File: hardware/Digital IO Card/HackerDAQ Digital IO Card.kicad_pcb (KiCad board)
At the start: 2 copper layers, 90 x 90 mm, 8 parts, among them J1 MiniFit_Jr_5569_08A2, J2 MiniFit_Jr_5569_08A2, J3 MiniFit_Jr_5569_08A2, J9 LD15S33E4GX00LF, U4 M95320-RMN6

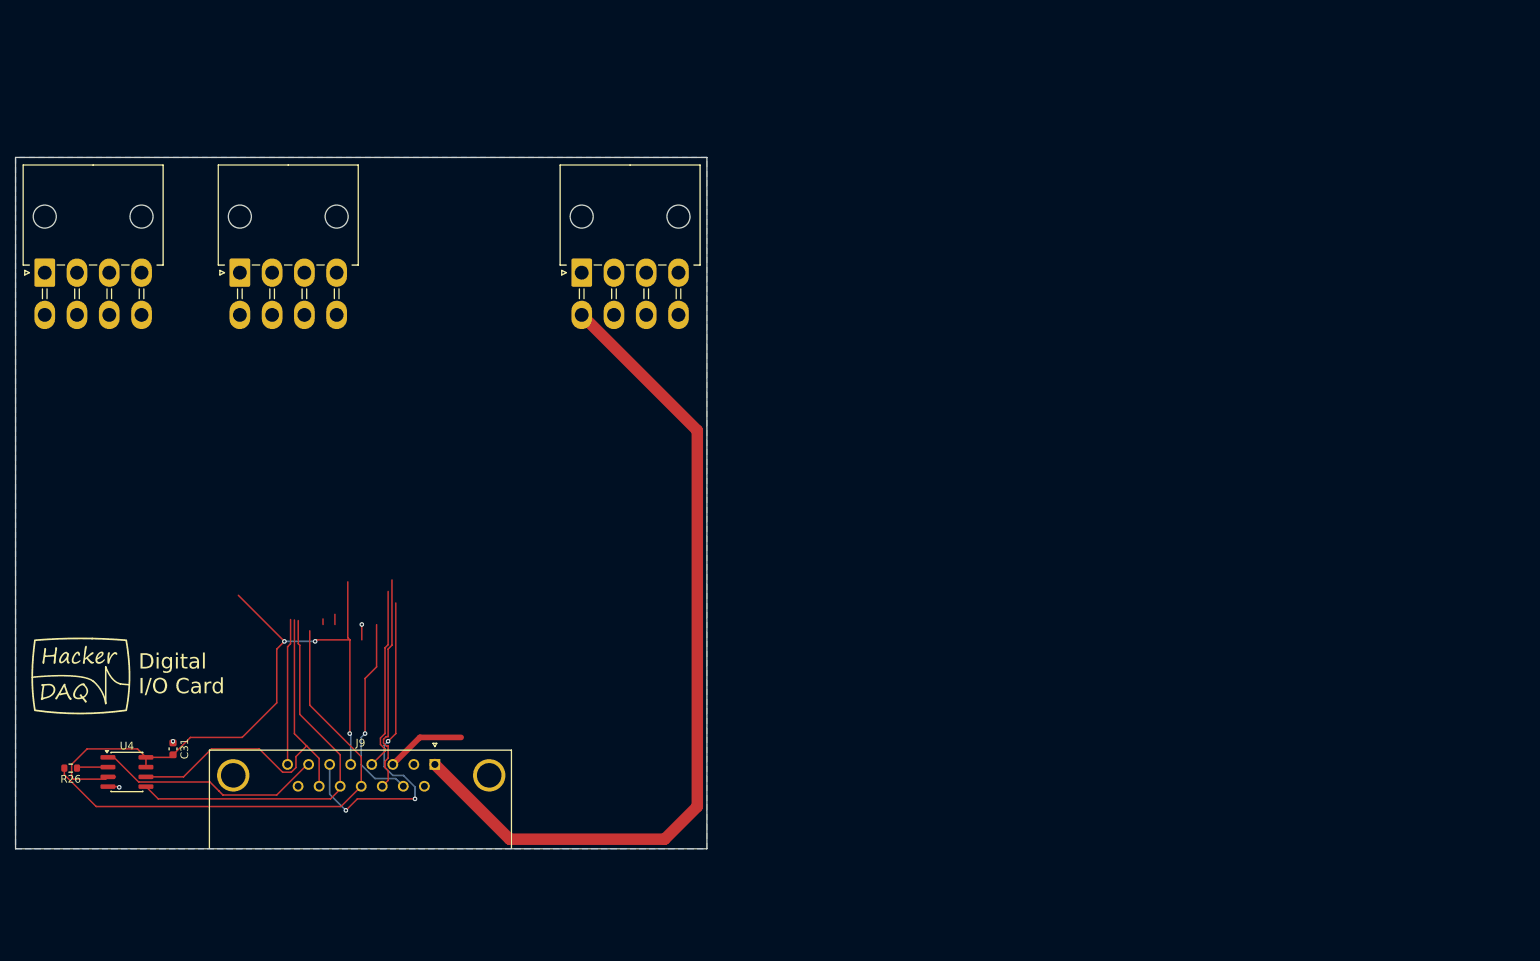
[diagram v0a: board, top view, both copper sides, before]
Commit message: DIO card initial schematic done
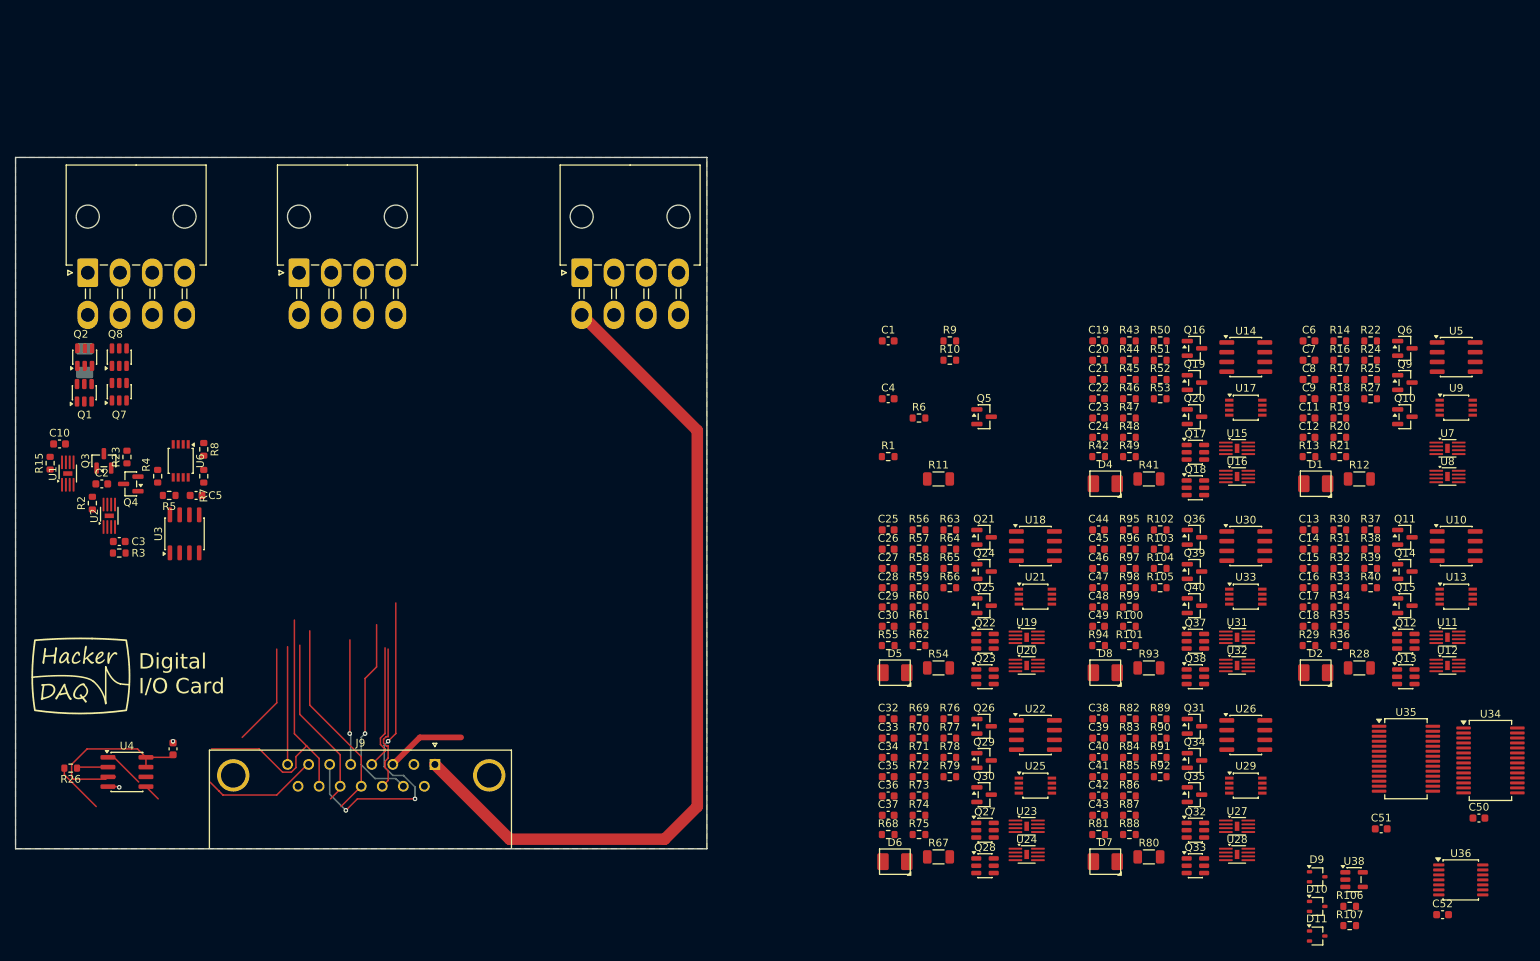
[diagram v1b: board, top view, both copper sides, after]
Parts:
- added C1: 1µF, Capacitor_SMD:C_0603_1608Metric, F.Cu at (163.6, 73.9)
- added C10: 1µF, Capacitor_SMD:C_0603_1608Metric, F.Cu at (55.7, 87.3)
- added C11: 1µF, Capacitor_SMD:C_0603_1608Metric, F.Cu at (218.4, 83.9)
- added C12: 100nF, Capacitor_SMD:C_0603_1608Metric, F.Cu at (218.4, 86.4)
- added C13: 100nF, Capacitor_SMD:C_0603_1608Metric, F.Cu at (218.4, 98.5)
- added C14: 1µF, Capacitor_SMD:C_0603_1608Metric, F.Cu at (218.4, 101.0)
- added C15: 1µF, Capacitor_SMD:C_0603_1608Metric, F.Cu at (218.4, 103.5)
- added C16: 1µF, Capacitor_SMD:C_0603_1608Metric, F.Cu at (218.4, 106.0)
- added C17: 1µF, Capacitor_SMD:C_0603_1608Metric, F.Cu at (218.4, 108.5)
- added C18: 100nF, Capacitor_SMD:C_0603_1608Metric, F.Cu at (218.4, 111.0)
- added C19: 100nF, Capacitor_SMD:C_0603_1608Metric, F.Cu at (191.0, 73.9)
- added C2: 1µF, Capacitor_SMD:C_0603_1608Metric, F.Cu at (61.2, 92.5)
- added C20: 1µF, Capacitor_SMD:C_0603_1608Metric, F.Cu at (191.0, 76.4)
- added C21: 1µF, Capacitor_SMD:C_0603_1608Metric, F.Cu at (191.0, 78.9)
- added C22: 1µF, Capacitor_SMD:C_0603_1608Metric, F.Cu at (191.0, 81.4)
- added C23: 1µF, Capacitor_SMD:C_0603_1608Metric, F.Cu at (191.0, 83.9)
- added C24: 100nF, Capacitor_SMD:C_0603_1608Metric, F.Cu at (191.0, 86.4)
- added C25: 100nF, Capacitor_SMD:C_0603_1608Metric, F.Cu at (163.6, 98.5)
- added C26: 1µF, Capacitor_SMD:C_0603_1608Metric, F.Cu at (163.6, 101.0)
- added C27: 1µF, Capacitor_SMD:C_0603_1608Metric, F.Cu at (163.6, 103.5)
- added C28: 1µF, Capacitor_SMD:C_0603_1608Metric, F.Cu at (163.6, 106.0)
- added C29: 1µF, Capacitor_SMD:C_0603_1608Metric, F.Cu at (163.6, 108.5)
- added C3: 1µF, Capacitor_SMD:C_0603_1608Metric, F.Cu at (63.5, 100.0)
- added C30: 100nF, Capacitor_SMD:C_0603_1608Metric, F.Cu at (163.6, 111.0)
- added C32: 100nF, Capacitor_SMD:C_0603_1608Metric, F.Cu at (163.6, 123.1)
- added C33: 1µF, Capacitor_SMD:C_0603_1608Metric, F.Cu at (163.6, 125.6)
- added C34: 1µF, Capacitor_SMD:C_0603_1608Metric, F.Cu at (163.6, 128.1)
- added C35: 1µF, Capacitor_SMD:C_0603_1608Metric, F.Cu at (163.6, 130.6)
- added C36: 1µF, Capacitor_SMD:C_0603_1608Metric, F.Cu at (163.6, 133.1)
- added C37: 100nF, Capacitor_SMD:C_0603_1608Metric, F.Cu at (163.6, 135.6)
- added C38: 100nF, Capacitor_SMD:C_0603_1608Metric, F.Cu at (191.0, 123.1)
- added C39: 1µF, Capacitor_SMD:C_0603_1608Metric, F.Cu at (191.0, 125.6)
- added C4: 100nF, Capacitor_SMD:C_0603_1608Metric, F.Cu at (163.6, 81.4)
- added C40: 1µF, Capacitor_SMD:C_0603_1608Metric, F.Cu at (191.0, 128.1)
- added C41: 1µF, Capacitor_SMD:C_0603_1608Metric, F.Cu at (191.0, 130.6)
- added C42: 1µF, Capacitor_SMD:C_0603_1608Metric, F.Cu at (191.0, 133.1)
- added C43: 100nF, Capacitor_SMD:C_0603_1608Metric, F.Cu at (191.0, 135.6)
- added C44: 100nF, Capacitor_SMD:C_0603_1608Metric, F.Cu at (191.0, 98.5)
- added C45: 1µF, Capacitor_SMD:C_0603_1608Metric, F.Cu at (191.0, 101.0)
- added C46: 1µF, Capacitor_SMD:C_0603_1608Metric, F.Cu at (191.0, 103.5)
- added C47: 1µF, Capacitor_SMD:C_0603_1608Metric, F.Cu at (191.0, 106.0)
- added C48: 1µF, Capacitor_SMD:C_0603_1608Metric, F.Cu at (191.0, 108.5)
- added C49: 100nF, Capacitor_SMD:C_0603_1608Metric, F.Cu at (191.0, 111.0)
- added C5: 100nF, Capacitor_SMD:C_0603_1608Metric, F.Cu at (73.5, 94.0)
- added C50: 100nF, Capacitor_SMD:C_0603_1608Metric, F.Cu at (240.5, 136.0)
- added C51: 100nF, Capacitor_SMD:C_0603_1608Metric, F.Cu at (227.8, 137.4)
- added C52: 100nF, Capacitor_SMD:C_0603_1608Metric, F.Cu at (235.8, 148.6)
- added C6: 100nF, Capacitor_SMD:C_0603_1608Metric, F.Cu at (218.4, 73.9)
- added C7: 1µF, Capacitor_SMD:C_0603_1608Metric, F.Cu at (218.4, 76.4)
- added C8: 1µF, Capacitor_SMD:C_0603_1608Metric, F.Cu at (218.4, 78.9)
- added C9: 1µF, Capacitor_SMD:C_0603_1608Metric, F.Cu at (218.4, 81.4)
- added D1: AA3528SURSK, ColorLEDs:AA3528, F.Cu at (219.2, 92.5)
- added D10: BAT54W, Package_TO_SOT_SMD:SOT-323_SC-70, F.Cu at (219.4, 147.5)
- added D11: BAT54W, Package_TO_SOT_SMD:SOT-323_SC-70, F.Cu at (219.4, 151.4)
- added D2: AA3528SURSK, ColorLEDs:AA3528, F.Cu at (219.2, 117.1)
- added D3: AA3528SURSK, ColorLEDs:AA3528, B.Cu at (59.0, 76.5)
- added D4: AA3528SURSK, ColorLEDs:AA3528, F.Cu at (191.9, 92.5)
- added D5: AA3528SURSK, ColorLEDs:AA3528, F.Cu at (164.5, 117.1)
- added D6: AA3528SURSK, ColorLEDs:AA3528, F.Cu at (164.5, 141.7)
- added D7: AA3528SURSK, ColorLEDs:AA3528, F.Cu at (191.9, 141.7)
- added D8: AA3528SURSK, ColorLEDs:AA3528, F.Cu at (191.9, 117.1)
- added D9: BAT54W, Package_TO_SOT_SMD:SOT-323_SC-70, F.Cu at (219.4, 143.6)
- added Q1: RVQ040N05, Package_TO_SOT_SMD:SOT-23-6, F.Cu at (59.0, 80.6)
- added Q10: 2N7002, Package_TO_SOT_SMD:SOT-23, F.Cu at (230.9, 83.8)
- added Q11: 2N7002, Package_TO_SOT_SMD:SOT-23, F.Cu at (230.9, 99.5)
- added Q12: RVQ040N05, Package_TO_SOT_SMD:SOT-23-6, F.Cu at (231.0, 113.0)
- added Q13: RVQ040N05, Package_TO_SOT_SMD:SOT-23-6, F.Cu at (231.0, 117.6)
- added Q14: 2N7002, Package_TO_SOT_SMD:SOT-23, F.Cu at (230.9, 103.9)
- added Q15: 2N7002, Package_TO_SOT_SMD:SOT-23, F.Cu at (230.9, 108.4)
- added Q16: 2N7002, Package_TO_SOT_SMD:SOT-23, F.Cu at (203.5, 74.9)
- added Q17: RVQ040N05, Package_TO_SOT_SMD:SOT-23-6, F.Cu at (203.6, 88.4)
- added Q18: RVQ040N05, Package_TO_SOT_SMD:SOT-23-6, F.Cu at (203.6, 93.0)
- added Q19: 2N7002, Package_TO_SOT_SMD:SOT-23, F.Cu at (203.5, 79.3)
- added Q2: RVQ040N05, Package_TO_SOT_SMD:SOT-23-6, F.Cu at (59.0, 76.0)
- added Q20: 2N7002, Package_TO_SOT_SMD:SOT-23, F.Cu at (203.5, 83.8)
- added Q21: 2N7002, Package_TO_SOT_SMD:SOT-23, F.Cu at (176.1, 99.5)
- added Q22: RVQ040N05, Package_TO_SOT_SMD:SOT-23-6, F.Cu at (176.2, 113.0)
- added Q23: RVQ040N05, Package_TO_SOT_SMD:SOT-23-6, F.Cu at (176.2, 117.6)
- added Q24: 2N7002, Package_TO_SOT_SMD:SOT-23, F.Cu at (176.1, 103.9)
- added Q25: 2N7002, Package_TO_SOT_SMD:SOT-23, F.Cu at (176.1, 108.4)
- added Q26: 2N7002, Package_TO_SOT_SMD:SOT-23, F.Cu at (176.1, 124.1)
- added Q27: RVQ040N05, Package_TO_SOT_SMD:SOT-23-6, F.Cu at (176.2, 137.6)
- added Q28: RVQ040N05, Package_TO_SOT_SMD:SOT-23-6, F.Cu at (176.2, 142.2)
- added Q29: 2N7002, Package_TO_SOT_SMD:SOT-23, F.Cu at (176.1, 128.5)
- added Q3: 2N7002, Package_TO_SOT_SMD:SOT-23, F.Cu at (61.5, 89.5)
- added Q30: 2N7002, Package_TO_SOT_SMD:SOT-23, F.Cu at (176.1, 133.0)
- added Q31: 2N7002, Package_TO_SOT_SMD:SOT-23, F.Cu at (203.5, 124.1)
- added Q32: RVQ040N05, Package_TO_SOT_SMD:SOT-23-6, F.Cu at (203.6, 137.6)
- added Q33: RVQ040N05, Package_TO_SOT_SMD:SOT-23-6, F.Cu at (203.6, 142.2)
- added Q34: 2N7002, Package_TO_SOT_SMD:SOT-23, F.Cu at (203.5, 128.5)
- added Q35: 2N7002, Package_TO_SOT_SMD:SOT-23, F.Cu at (203.5, 133.0)
- added Q36: 2N7002, Package_TO_SOT_SMD:SOT-23, F.Cu at (203.5, 99.5)
- added Q37: RVQ040N05, Package_TO_SOT_SMD:SOT-23-6, F.Cu at (203.6, 113.0)
- added Q38: RVQ040N05, Package_TO_SOT_SMD:SOT-23-6, F.Cu at (203.6, 117.6)
- added Q39: 2N7002, Package_TO_SOT_SMD:SOT-23, F.Cu at (203.5, 103.9)
- added Q4: 2N7002, Package_TO_SOT_SMD:SOT-23, F.Cu at (65.0, 92.5)
- added Q40: 2N7002, Package_TO_SOT_SMD:SOT-23, F.Cu at (203.5, 108.4)
- added Q5: 2N7002, Package_TO_SOT_SMD:SOT-23, F.Cu at (176.1, 83.8)
- added Q6: 2N7002, Package_TO_SOT_SMD:SOT-23, F.Cu at (230.9, 74.9)
- added Q7: RVQ040N05, Package_TO_SOT_SMD:SOT-23-6, F.Cu at (63.5, 80.5)
- added Q8: RVQ040N05, Package_TO_SOT_SMD:SOT-23-6, F.Cu at (63.5, 76.0)
- added Q9: 2N7002, Package_TO_SOT_SMD:SOT-23, F.Cu at (230.9, 79.3)
- added R1: 2.2, Resistor_SMD:R_0603_1608Metric, F.Cu at (163.6, 88.9)
- added R10: 14.7k, Resistor_SMD:R_0603_1608Metric, F.Cu at (171.6, 76.4)
- added R100: 14.7k, Resistor_SMD:R_0603_1608Metric, F.Cu at (195.0, 111.0)
- added R101: 1, Resistor_SMD:R_0603_1608Metric, F.Cu at (195.0, 113.5)
- added R102: 1, Resistor_SMD:R_0603_1608Metric, F.Cu at (199.0, 98.5)
- added R103: 133k, Resistor_SMD:R_0603_1608Metric, F.Cu at (199.0, 101.0)
- added R104: 33.2k, Resistor_SMD:R_0603_1608Metric, F.Cu at (199.0, 103.5)
- added R105: 10k, Resistor_SMD:R_0603_1608Metric, F.Cu at (199.0, 106.0)
- added R106: 10k, Resistor_SMD:R_0603_1608Metric, F.Cu at (223.7, 147.5)
- added R107: 33, Resistor_SMD:R_0603_1608Metric, F.Cu at (223.7, 150.0)
- added R11: 150, Resistor_SMD:R_1206_3216Metric, F.Cu at (170.2, 91.9)
- added R12: 150, Resistor_SMD:R_1206_3216Metric, F.Cu at (224.9, 91.9)
- added R13: 10k, Resistor_SMD:R_0603_1608Metric, F.Cu at (218.4, 88.9)
- added R14: 75k, Resistor_SMD:R_0603_1608Metric, F.Cu at (222.4, 73.9)
- added R15: 1, Resistor_SMD:R_0603_1608Metric, F.Cu at (54.5, 89.8)
- added R16: 2.2, Resistor_SMD:R_0603_1608Metric, F.Cu at (222.4, 76.4)
- added R17: 2.2, Resistor_SMD:R_0603_1608Metric, F.Cu at (222.4, 78.9)
- added R18: 30k, Resistor_SMD:R_0603_1608Metric, F.Cu at (222.4, 81.4)
- added R19: 133k, Resistor_SMD:R_0603_1608Metric, F.Cu at (222.4, 83.9)
- added R2: 1, Resistor_SMD:R_0603_1608Metric, F.Cu at (60.0, 95.0)
- added R20: 14.7k, Resistor_SMD:R_0603_1608Metric, F.Cu at (222.4, 86.4)
- added R21: 1, Resistor_SMD:R_0603_1608Metric, F.Cu at (222.4, 88.9)
- added R22: 1, Resistor_SMD:R_0603_1608Metric, F.Cu at (226.4, 73.9)
- added R23: 10k, Resistor_SMD:R_0603_1608Metric, F.Cu at (64.5, 89.0)
- added R24: 133k, Resistor_SMD:R_0603_1608Metric, F.Cu at (226.4, 76.4)
- added R25: 33.2k, Resistor_SMD:R_0603_1608Metric, F.Cu at (226.4, 78.9)
- added R27: 10k, Resistor_SMD:R_0603_1608Metric, F.Cu at (226.4, 81.4)
- added R28: 150, Resistor_SMD:R_1206_3216Metric, F.Cu at (224.9, 116.5)
- added R29: 10k, Resistor_SMD:R_0603_1608Metric, F.Cu at (218.4, 113.5)
- added R3: 2.2, Resistor_SMD:R_0603_1608Metric, F.Cu at (63.5, 101.5)
- added R30: 75k, Resistor_SMD:R_0603_1608Metric, F.Cu at (222.4, 98.5)
- added R31: 2.2, Resistor_SMD:R_0603_1608Metric, F.Cu at (222.4, 101.0)
- added R32: 2.2, Resistor_SMD:R_0603_1608Metric, F.Cu at (222.4, 103.5)
- added R33: 30k, Resistor_SMD:R_0603_1608Metric, F.Cu at (222.4, 106.0)
- added R34: 133k, Resistor_SMD:R_0603_1608Metric, F.Cu at (222.4, 108.5)
- added R35: 14.7k, Resistor_SMD:R_0603_1608Metric, F.Cu at (222.4, 111.0)
- added R36: 1, Resistor_SMD:R_0603_1608Metric, F.Cu at (222.4, 113.5)
- added R37: 1, Resistor_SMD:R_0603_1608Metric, F.Cu at (226.4, 98.5)
- added R38: 133k, Resistor_SMD:R_0603_1608Metric, F.Cu at (226.4, 101.0)
- added R39: 33.2k, Resistor_SMD:R_0603_1608Metric, F.Cu at (226.4, 103.5)
- added R4: 75k, Resistor_SMD:R_0603_1608Metric, F.Cu at (68.5, 91.5)
- added R40: 10k, Resistor_SMD:R_0603_1608Metric, F.Cu at (226.4, 106.0)
- added R41: 150, Resistor_SMD:R_1206_3216Metric, F.Cu at (197.5, 91.9)
- added R42: 10k, Resistor_SMD:R_0603_1608Metric, F.Cu at (191.0, 88.9)
- added R43: 75k, Resistor_SMD:R_0603_1608Metric, F.Cu at (195.0, 73.9)
- added R44: 2.2, Resistor_SMD:R_0603_1608Metric, F.Cu at (195.0, 76.4)
- added R45: 2.2, Resistor_SMD:R_0603_1608Metric, F.Cu at (195.0, 78.9)
- added R46: 30k, Resistor_SMD:R_0603_1608Metric, F.Cu at (195.0, 81.4)
- added R47: 133k, Resistor_SMD:R_0603_1608Metric, F.Cu at (195.0, 83.9)
- added R48: 14.7k, Resistor_SMD:R_0603_1608Metric, F.Cu at (195.0, 86.4)
- added R49: 1, Resistor_SMD:R_0603_1608Metric, F.Cu at (195.0, 88.9)
- added R5: 30k, Resistor_SMD:R_0603_1608Metric, F.Cu at (70.0, 94.0)
- added R50: 1, Resistor_SMD:R_0603_1608Metric, F.Cu at (199.0, 73.9)
- added R51: 133k, Resistor_SMD:R_0603_1608Metric, F.Cu at (199.0, 76.4)
- added R52: 33.2k, Resistor_SMD:R_0603_1608Metric, F.Cu at (199.0, 78.9)
- added R53: 10k, Resistor_SMD:R_0603_1608Metric, F.Cu at (199.0, 81.4)
- added R54: 150, Resistor_SMD:R_1206_3216Metric, F.Cu at (170.2, 116.5)
- added R55: 10k, Resistor_SMD:R_0603_1608Metric, F.Cu at (163.6, 113.5)
- added R56: 75k, Resistor_SMD:R_0603_1608Metric, F.Cu at (167.6, 98.5)
- added R57: 2.2, Resistor_SMD:R_0603_1608Metric, F.Cu at (167.6, 101.0)
- added R58: 2.2, Resistor_SMD:R_0603_1608Metric, F.Cu at (167.6, 103.5)
- added R59: 30k, Resistor_SMD:R_0603_1608Metric, F.Cu at (167.6, 106.0)
- added R6: 10k, Resistor_SMD:R_0603_1608Metric, F.Cu at (167.6, 83.9)
- added R60: 133k, Resistor_SMD:R_0603_1608Metric, F.Cu at (167.6, 108.5)
- added R61: 14.7k, Resistor_SMD:R_0603_1608Metric, F.Cu at (167.6, 111.0)
- added R62: 1, Resistor_SMD:R_0603_1608Metric, F.Cu at (167.6, 113.5)
- added R63: 1, Resistor_SMD:R_0603_1608Metric, F.Cu at (171.6, 98.5)
- added R64: 133k, Resistor_SMD:R_0603_1608Metric, F.Cu at (171.6, 101.0)
- added R65: 33.2k, Resistor_SMD:R_0603_1608Metric, F.Cu at (171.6, 103.5)
- added R66: 10k, Resistor_SMD:R_0603_1608Metric, F.Cu at (171.6, 106.0)
- added R67: 150, Resistor_SMD:R_1206_3216Metric, F.Cu at (170.2, 141.1)
- added R68: 10k, Resistor_SMD:R_0603_1608Metric, F.Cu at (163.6, 138.1)
- added R69: 75k, Resistor_SMD:R_0603_1608Metric, F.Cu at (167.6, 123.1)
- added R7: 33.2k, Resistor_SMD:R_0603_1608Metric, F.Cu at (74.5, 91.5)
- added R70: 2.2, Resistor_SMD:R_0603_1608Metric, F.Cu at (167.6, 125.6)
- added R71: 2.2, Resistor_SMD:R_0603_1608Metric, F.Cu at (167.6, 128.1)
- added R72: 30k, Resistor_SMD:R_0603_1608Metric, F.Cu at (167.6, 130.6)
- added R73: 133k, Resistor_SMD:R_0603_1608Metric, F.Cu at (167.6, 133.1)
- added R74: 14.7k, Resistor_SMD:R_0603_1608Metric, F.Cu at (167.6, 135.6)
- added R75: 1, Resistor_SMD:R_0603_1608Metric, F.Cu at (167.6, 138.1)
- added R76: 1, Resistor_SMD:R_0603_1608Metric, F.Cu at (171.6, 123.1)
- added R77: 133k, Resistor_SMD:R_0603_1608Metric, F.Cu at (171.6, 125.6)
- added R78: 33.2k, Resistor_SMD:R_0603_1608Metric, F.Cu at (171.6, 128.1)
- added R79: 10k, Resistor_SMD:R_0603_1608Metric, F.Cu at (171.6, 130.6)
- added R8: 133k, Resistor_SMD:R_0603_1608Metric, F.Cu at (74.5, 88.0)
- added R80: 150, Resistor_SMD:R_1206_3216Metric, F.Cu at (197.5, 141.1)
- added R81: 10k, Resistor_SMD:R_0603_1608Metric, F.Cu at (191.0, 138.1)
- added R82: 75k, Resistor_SMD:R_0603_1608Metric, F.Cu at (195.0, 123.1)
- added R83: 2.2, Resistor_SMD:R_0603_1608Metric, F.Cu at (195.0, 125.6)
- added R84: 2.2, Resistor_SMD:R_0603_1608Metric, F.Cu at (195.0, 128.1)
- added R85: 30k, Resistor_SMD:R_0603_1608Metric, F.Cu at (195.0, 130.6)
- added R86: 133k, Resistor_SMD:R_0603_1608Metric, F.Cu at (195.0, 133.1)
- added R87: 14.7k, Resistor_SMD:R_0603_1608Metric, F.Cu at (195.0, 135.6)
- added R88: 1, Resistor_SMD:R_0603_1608Metric, F.Cu at (195.0, 138.1)
- added R89: 1, Resistor_SMD:R_0603_1608Metric, F.Cu at (199.0, 123.1)
- added R9: 133k, Resistor_SMD:R_0603_1608Metric, F.Cu at (171.6, 73.9)
- added R90: 133k, Resistor_SMD:R_0603_1608Metric, F.Cu at (199.0, 125.6)
- added R91: 33.2k, Resistor_SMD:R_0603_1608Metric, F.Cu at (199.0, 128.1)
- added R92: 10k, Resistor_SMD:R_0603_1608Metric, F.Cu at (199.0, 130.6)
- added R93: 150, Resistor_SMD:R_1206_3216Metric, F.Cu at (197.5, 116.5)
- added R94: 10k, Resistor_SMD:R_0603_1608Metric, F.Cu at (191.0, 113.5)
- added R95: 75k, Resistor_SMD:R_0603_1608Metric, F.Cu at (195.0, 98.5)
- added R96: 2.2, Resistor_SMD:R_0603_1608Metric, F.Cu at (195.0, 101.0)
- added R97: 2.2, Resistor_SMD:R_0603_1608Metric, F.Cu at (195.0, 103.5)
- added R98: 30k, Resistor_SMD:R_0603_1608Metric, F.Cu at (195.0, 106.0)
- added R99: 133k, Resistor_SMD:R_0603_1608Metric, F.Cu at (195.0, 108.5)
- added U1: RT9624CGQWA, Project Library:DFN-8-1EP_2x2mm_P0.5mm_EP0.6x1.2mm_LeadsExtended, F.Cu at (56.8, 91.2)
- added U10: LM311DR, Package_SO:SOIC-8_3.9x4.9mm_P1.27mm, F.Cu at (237.5, 100.6)
- added U11: RT9624CGQWA, Project Library:DFN-8-1EP_2x2mm_P0.5mm_EP0.6x1.2mm_LeadsExtended, F.Cu at (236.4, 112.5)
- added U12: RT9624CGQWA, Project Library:DFN-8-1EP_2x2mm_P0.5mm_EP0.6x1.2mm_LeadsExtended, F.Cu at (236.4, 116.1)
- added U13: LM358, Package_SO:TSSOP-8_3x3mm_P0.65mm, F.Cu at (237.5, 107.2)
- added U14: LM311DR, Package_SO:SOIC-8_3.9x4.9mm_P1.27mm, F.Cu at (210.2, 76.0)
- added U15: RT9624CGQWA, Project Library:DFN-8-1EP_2x2mm_P0.5mm_EP0.6x1.2mm_LeadsExtended, F.Cu at (209.0, 87.9)
- added U16: RT9624CGQWA, Project Library:DFN-8-1EP_2x2mm_P0.5mm_EP0.6x1.2mm_LeadsExtended, F.Cu at (209.0, 91.5)
- added U17: LM358, Package_SO:TSSOP-8_3x3mm_P0.65mm, F.Cu at (210.2, 82.6)
- added U18: LM311DR, Package_SO:SOIC-8_3.9x4.9mm_P1.27mm, F.Cu at (182.8, 100.6)
- added U19: RT9624CGQWA, Project Library:DFN-8-1EP_2x2mm_P0.5mm_EP0.6x1.2mm_LeadsExtended, F.Cu at (181.6, 112.5)
- added U2: RT9624CGQWA, Project Library:DFN-8-1EP_2x2mm_P0.5mm_EP0.6x1.2mm_LeadsExtended, F.Cu at (62.2, 96.7)
- added U20: RT9624CGQWA, Project Library:DFN-8-1EP_2x2mm_P0.5mm_EP0.6x1.2mm_LeadsExtended, F.Cu at (181.6, 116.1)
- added U21: LM358, Package_SO:TSSOP-8_3x3mm_P0.65mm, F.Cu at (182.8, 107.2)
- added U22: LM311DR, Package_SO:SOIC-8_3.9x4.9mm_P1.27mm, F.Cu at (182.8, 125.2)
- added U23: RT9624CGQWA, Project Library:DFN-8-1EP_2x2mm_P0.5mm_EP0.6x1.2mm_LeadsExtended, F.Cu at (181.6, 137.1)
- added U24: RT9624CGQWA, Project Library:DFN-8-1EP_2x2mm_P0.5mm_EP0.6x1.2mm_LeadsExtended, F.Cu at (181.6, 140.7)
- added U25: LM358, Package_SO:TSSOP-8_3x3mm_P0.65mm, F.Cu at (182.8, 131.8)
- added U26: LM311DR, Package_SO:SOIC-8_3.9x4.9mm_P1.27mm, F.Cu at (210.2, 125.2)
- added U27: RT9624CGQWA, Project Library:DFN-8-1EP_2x2mm_P0.5mm_EP0.6x1.2mm_LeadsExtended, F.Cu at (209.0, 137.1)
- added U28: RT9624CGQWA, Project Library:DFN-8-1EP_2x2mm_P0.5mm_EP0.6x1.2mm_LeadsExtended, F.Cu at (209.0, 140.7)
- added U29: LM358, Package_SO:TSSOP-8_3x3mm_P0.65mm, F.Cu at (210.2, 131.8)
- added U3: LM311DR, Package_SO:SOIC-8_3.9x4.9mm_P1.27mm, F.Cu at (72.0, 99.0)
- added U30: LM311DR, Package_SO:SOIC-8_3.9x4.9mm_P1.27mm, F.Cu at (210.2, 100.6)
- added U31: RT9624CGQWA, Project Library:DFN-8-1EP_2x2mm_P0.5mm_EP0.6x1.2mm_LeadsExtended, F.Cu at (209.0, 112.5)
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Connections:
- C31 pad 1: +3.3V -> +5V
- J1 pad 1: V_LOGIC -> /V_{LOGIC}_PORTA
- J1 pad 2: V_LOGIC -> /V_{LOGIC}_PORTB
- J2 pad 1: unconnected-(J2-Pin_1-Pad1) -> GND
- J2 pad 2: unconnected-(J2-Pin_2-Pad2) -> GND
- J2 pad 3: unconnected-(J2-Pin_3-Pad3) -> GND
- J2 pad 4: unconnected-(J2-Pin_4-Pad4) -> GND
- J2 pad 5: unconnected-(J2-Pin_5-Pad5) -> /DIOA0
- J2 pad 6: unconnected-(J2-Pin_6-Pad6) -> /DIOA1
- J2 pad 7: unconnected-(J2-Pin_7-Pad7) -> /DIOA2
- J2 pad 8: unconnected-(J2-Pin_8-Pad8) -> /DIOA3
- J3 pad 1: unconnected-(J3-Pin_1-Pad1) -> GND
- J3 pad 2: unconnected-(J3-Pin_2-Pad2) -> GND
- J3 pad 3: unconnected-(J3-Pin_3-Pad3) -> GND
- J3 pad 4: unconnected-(J3-Pin_4-Pad4) -> GND
- J3 pad 5: unconnected-(J3-Pin_5-Pad5) -> /DIOB0
- J3 pad 6: unconnected-(J3-Pin_6-Pad6) -> /DIOB1
- J3 pad 7: unconnected-(J3-Pin_7-Pad7) -> /DIOB2
- J3 pad 8: unconnected-(J3-Pin_8-Pad8) -> /DIOB3
- J9 pad 12: /B2B Connector Card Side/SPI.MISO -> /SPI.MISO
- J9 pad 13: /B2B Connector Card Side/SPI.MOSI -> /SPI.MOSI
- J9 pad 14: /B2B Connector Card Side/SPI.SCLK -> /SPI.SCLK
- J9 pad 15: /B2B Connector Card Side/CS1 -> /~{CS}1
- J9 pad 6: /B2B Connector Card Side/~{RESET} -> /~{RESET}
- J9 pad 7: /B2B Connector Card Side/CS2 -> /~{CS}2
- J9 pad 8: /B2B Connector Card Side/CS0 -> /~{CS}0
- R26 pad 2: /B2B Connector Card Side/SPI.MISO -> /IOExpanderA/SPI_5V.MISO
- U4 pad 1: /B2B Connector Card Side/CS2 -> /LevelShifter/~{CS_5V}2
- U4 pad 3: +3.3V -> +5V
- U4 pad 5: /B2B Connector Card Side/SPI.MOSI -> /IOExpanderA/SPI_5V.MOSI
- U4 pad 6: /B2B Connector Card Side/SPI.SCLK -> /IOExpanderA/SPI_5V.SCLK
- U4 pad 7: +3.3V -> +5V
- U4 pad 8: +3.3V -> +5V
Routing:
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
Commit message: Start redoing DIO card
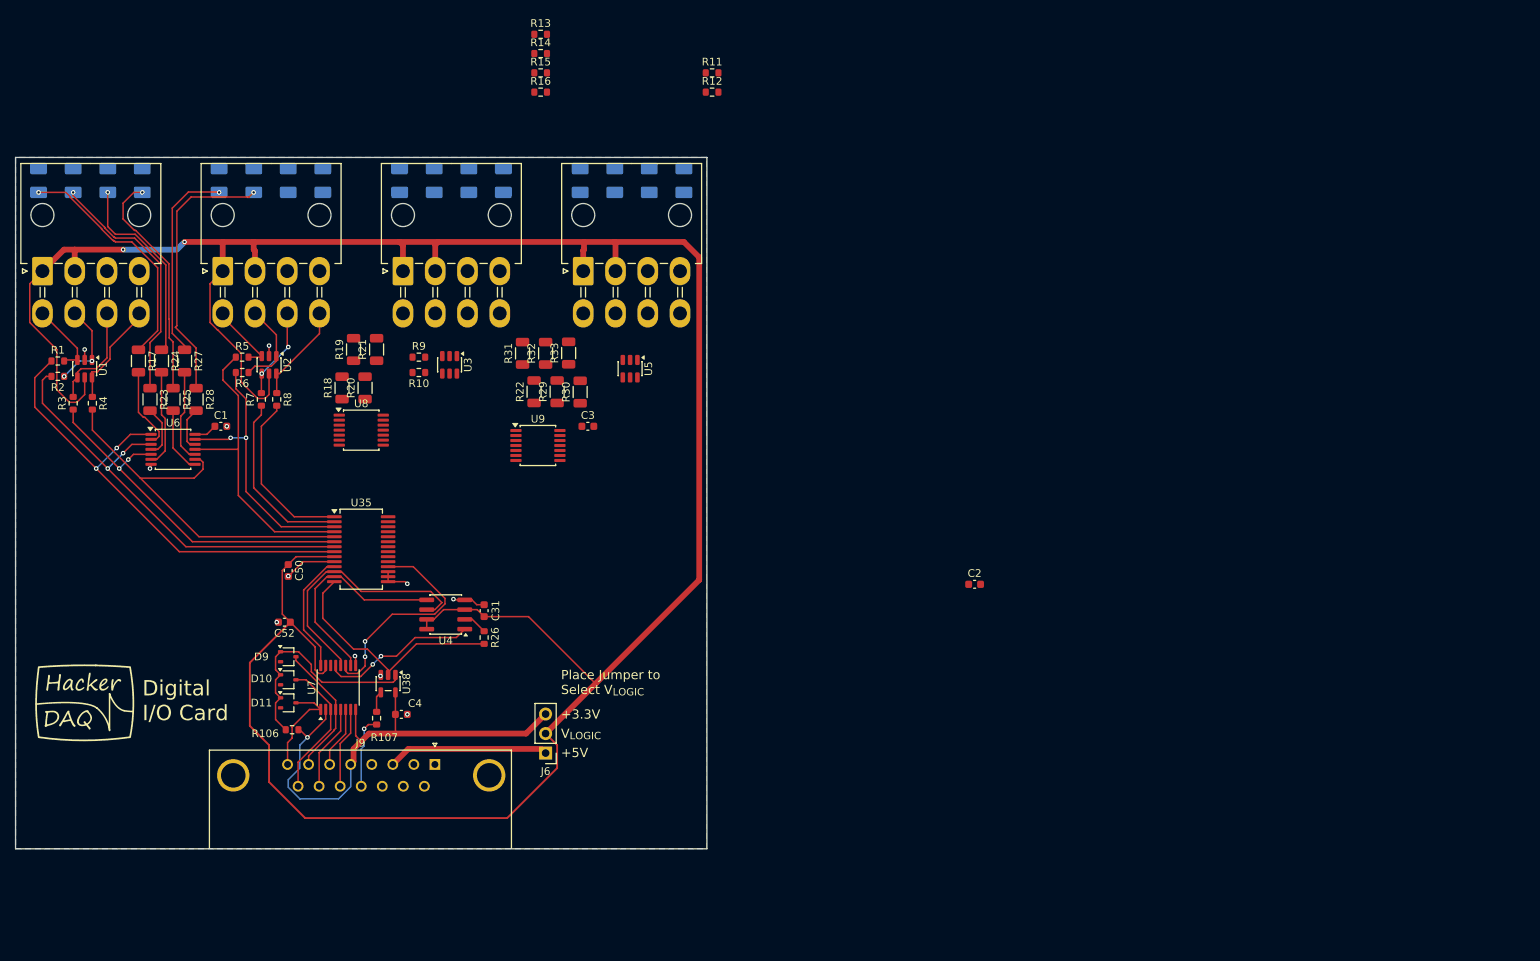
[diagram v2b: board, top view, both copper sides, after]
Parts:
- removed C10, C11, C14, C15, C16, C17, C20, C21, C22, C23, C26, C27, C28, C29, C33, C34, C35, C36, C39, C40, C41, C42, C45, C46, C47, C48, C7, C8, C9: 1µF, Capacitor_SMD:C_0603_1608Metric
- removed C12, C13, C18, C19, C24, C25, C30, C32, C37, C38, C43, C44, C49, C5, C51, C6: 100nF, Capacitor_SMD:C_0603_1608Metric
- removed J1: MiniFit_Jr_5569_08A2, Project Library:Molex_Mini-Fit_Jr_5569-08A2_2x04_P4.20mm_Horizontal
- removed Q1, Q12, Q13, Q17, Q18, Q2, Q22, Q23, Q27, Q28, Q32, Q33, Q37, Q38, Q7, Q8: RVQ040N05, Package_TO_SOT_SMD:SOT-23-6
- removed Q10, Q11, Q14, Q15, Q16, Q19, Q20, Q21, Q24, Q25, Q26, Q29, Q3, Q30, Q31, Q34, Q35, Q36, Q39, Q4, Q40, Q5, Q6, Q9: 2N7002, Package_TO_SOT_SMD:SOT-23
- removed R100, R35, R48, R61, R74, R87: 14.7k, Resistor_SMD:R_0603_1608Metric
- removed R101, R102, R36, R37, R49, R50, R62, R63, R75, R76, R88, R89: 1, Resistor_SMD:R_0603_1608Metric
- removed R103, R34, R38, R47, R51, R60, R64, R73, R77, R86, R90, R99: 133k, Resistor_SMD:R_0603_1608Metric
- removed R104, R39, R52, R65, R78, R91: 33.2k, Resistor_SMD:R_0603_1608Metric
- removed R105, R40, R42, R53, R55, R66, R68, R79, R81, R92, R94: 10k, Resistor_SMD:R_0603_1608Metric
- removed R41, R54, R67, R80, R93: 150, Resistor_SMD:R_1206_3216Metric
- removed R43, R56, R69, R82, R95: 75k, Resistor_SMD:R_0603_1608Metric
- removed R44, R45, R57, R58, R70, R71, R83, R84, R96, R97: 2.2, Resistor_SMD:R_0603_1608Metric
- removed R46, R59, R72, R85, R98: 30k, Resistor_SMD:R_0603_1608Metric
- removed U10, U14, U18, U22, U26, U30: LM311DR, Package_SO:SOIC-8_3.9x4.9mm_P1.27mm
- removed U11, U12, U15, U16, U19, U20, U23, U24, U27, U28, U31, U32: RT9624CGQWA, Project Library:DFN-8-1EP_2x2mm_P0.5mm_EP0.6x1.2mm_LeadsExtended
- removed U13, U17, U21, U25, U29, U33: LM358, Package_SO:TSSOP-8_3x3mm_P0.65mm
- removed U34: MCP23S17_SS, Package_SO:SSOP-28_5.3x10.2mm_P0.65mm
- removed U36: SN74ACT17PWR, Package_SO:TSSOP-14_4.4x5mm_P0.65mm
- added D12: AA3528SURSK, ColorLEDs:AA3528, B.Cu at (113.5, 53.0)
- added D13: AA3528SURSK, ColorLEDs:AA3528, B.Cu at (85.5, 53.0)
- added D14: AA3528SURSK, ColorLEDs:AA3528, B.Cu at (100.0, 53.0)
- added D15: AA3528SURSK, ColorLEDs:AA3528, B.Cu at (128.0, 53.0)
- added D16: AA3528SURSK, ColorLEDs:AA3528, B.Cu at (137.0, 53.0)
- added D17: AA3528SURSK, ColorLEDs:AA3528, B.Cu at (109.0, 53.0)
- added D18: AA3528SURSK, ColorLEDs:AA3528, B.Cu at (123.5, 53.0)
- added D19: AA3528SURSK, ColorLEDs:AA3528, B.Cu at (132.5, 53.0)
- added J4: MiniFit_Jr_5569_08A2, Project Library:Molex_Mini-Fit_Jr_5569-08A2_2x04_P4.20mm_Horizontal, F.Cu at (106.7, 64.8)
- added J5: MiniFit_Jr_5569_08A2, Project Library:Molex_Mini-Fit_Jr_5569-08A2_2x04_P4.20mm_Horizontal, F.Cu at (130.2, 64.8)
- added J6: HEADER_3x1, Connector_PinHeader_2.54mm:PinHeader_1x03_P2.54mm_Vertical, F.Cu at (119.0, 127.5)
- C1, C2, C3: value 1µF -> 100nF
- D1, D2, D4, D5, D6, D7, D8: moved to B.Cu
- R1, R16, R3: value 2.2 -> 33
- R10: value 14.7k -> 33
- R11, R12: value 150 -> 33; footprint Resistor_SMD:R_1206_3216Metric -> Resistor_SMD:R_0603_1608Metric
- R13, R6: value 10k -> 33
- R14, R4: value 75k -> 33
- R15, R2: value 1 -> 33
- R17, R31, R32: value 2.2 -> 150; footprint Resistor_SMD:R_0603_1608Metric -> Resistor_SMD:R_1206_3216Metric
- R18, R33: value 30k -> 150; footprint Resistor_SMD:R_0603_1608Metric -> Resistor_SMD:R_1206_3216Metric
- R19, R24: value 133k -> 150; footprint Resistor_SMD:R_0603_1608Metric -> Resistor_SMD:R_1206_3216Metric
- R20: value 14.7k -> 150; footprint Resistor_SMD:R_0603_1608Metric -> Resistor_SMD:R_1206_3216Metric
- R21, R22: value 1 -> 150; footprint Resistor_SMD:R_0603_1608Metric -> Resistor_SMD:R_1206_3216Metric
- R23, R27, R29: value 10k -> 150; footprint Resistor_SMD:R_0603_1608Metric -> Resistor_SMD:R_1206_3216Metric
- R25: value 33.2k -> 150; footprint Resistor_SMD:R_0603_1608Metric -> Resistor_SMD:R_1206_3216Metric
- R30: value 75k -> 150; footprint Resistor_SMD:R_0603_1608Metric -> Resistor_SMD:R_1206_3216Metric
- R5: value 30k -> 33
- R7: value 33.2k -> 33
- R8, R9: value 133k -> 33
- U1, U2: value RT9624CGQWA -> SRV05-4.TCT; footprint Project Library:DFN-8-1EP_2x2mm_P0.5mm_EP0.6x1.2mm_LeadsExtended -> Package_TO_SOT_SMD:SOT-23-6
- U3, U5: value LM311DR -> SRV05-4.TCT; footprint Package_SO:SOIC-8_3.9x4.9mm_P1.27mm -> Package_TO_SOT_SMD:SOT-23-6
- U6, U9: value LM358 -> SN74ACT17PWR; footprint Package_SO:TSSOP-8_3x3mm_P0.65mm -> Package_SO:TSSOP-14_4.4x5mm_P0.65mm
- U7: value RT9624CGQWA -> TXB0106PW; footprint Project Library:DFN-8-1EP_2x2mm_P0.5mm_EP0.6x1.2mm_LeadsExtended -> Package_SO:TSSOP-16_4.4x5mm_P0.65mm
- U8: value RT9624CGQWA -> SN74ACT17PWR; footprint Project Library:DFN-8-1EP_2x2mm_P0.5mm_EP0.6x1.2mm_LeadsExtended -> Package_SO:TSSOP-14_4.4x5mm_P0.65mm
- moved D2 174.0 mm to (57.5, 53.0), turned to 90 degrees
- moved D1 170.9 mm to (53.0, 53.0), turned to 90 degrees
- moved C50 158.3 mm to (85.5, 103.8), turned to -90 degrees
- moved R24 157.4 mm to (69.0, 76.5), turned to -90 degrees
- moved R17 156.4 mm to (66.0, 76.5), turned to -90 degrees
- moved R25 155.9 mm to (70.5, 81.5), turned to -90 degrees
- moved C52 155.5 mm to (85.0, 110.5), turned to 180 degrees
- moved R28 155.4 mm to (73.5, 81.5), turned to -90 degrees
- moved R27 154.5 mm to (72.0, 76.5), turned to -90 degrees
- moved U7 147.7 mm to (92.0, 119.0), turned to 90 degrees
- moved U8 141.5 mm to (95.0, 85.5)
- moved R106 139.6 mm to (86.0, 124.5)
- moved U35 138.7 mm to (95.0, 101.0)
- moved D11 137.3 mm to (85.5, 121.0)
- moved D10 137.2 mm to (85.5, 118.0)
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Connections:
- net /IOExpanderA/SPI_5V.MISO renamed /SPI_VL.MISO
- C1 pad 1: Net-(U1-VCC) -> +5V
- C2 pad 1: Net-(C2-Pad1) -> +5V
- C2 pad 2: /DigitalIODriverA0/PULL_PHASE -> GND
- C3 pad 1: Net-(U2-VCC) -> +5V
- C31 pad 1: +5V -> V_{LOGIC}
- C4 pad 1: +5V -> +3.3V
- C50 pad 1: +5V -> V_{LOGIC}
- C52 pad 1: +5V -> V_{LOGIC}
- D1 pad 1: Net-(D1-K) -> GND
- D2 pad 1: Net-(D2-K) -> GND
- D3 pad 1: Net-(D3-K) -> GND
- D4 pad 1: Net-(D4-K) -> GND
- D5 pad 1: Net-(D5-K) -> GND
- D6 pad 1: Net-(D6-K) -> GND
- D7 pad 1: Net-(D7-K) -> GND
- D8 pad 1: Net-(D8-K) -> GND
- J2 pad 1: GND -> V_{LOGIC}
- J2 pad 2: GND -> V_{LOGIC}
- J2 pad 5: /DIOA0 -> /IO0
- J2 pad 6: /DIOA1 -> /IO1
- J2 pad 7: /DIOA2 -> /IO2
- J2 pad 8: /DIOA3 -> /IO3
- J3 pad 1: GND -> V_{LOGIC}
- J3 pad 2: GND -> V_{LOGIC}
- J3 pad 5: /DIOB0 -> /IO4
- J3 pad 6: /DIOB1 -> /IO5
- J3 pad 7: /DIOB2 -> /IO6
- J3 pad 8: /DIOB3 -> /IO7
- R1 pad 1: +5V -> /IOExpander/PB7
- R1 pad 2: Net-(U1-VCC) -> /IO0
- R10 pad 1: /DigitalIODriverA0/V_{LOGIC}/10 -> /IO9
- R10 pad 2: GND -> /IOExpander/PA6
- R11 pad 1: +5V -> /IOExpander/PA5
- R11 pad 2: Net-(D3-A) -> /IO10
- R12 pad 1: +5V -> /IO11
- R12 pad 2: Net-(D1-A) -> /IOExpander/PA4
- R13 pad 1: /DIG_IN_A1 -> /IOExpander/PA3
- R13 pad 2: +5V -> /IO12
- R14 pad 1: /DIG_IN_A1 -> /IO13
- R14 pad 2: Net-(U5-+) -> /IOExpander/PA2
- R15 pad 1: Net-(U1-BOOT) -> /IOExpander/PA1
- R15 pad 2: Net-(C10-Pad1) -> /IO14
- R16 pad 1: +5V -> /IO15
- R16 pad 2: Net-(U7-VCC) -> /IOExpander/PA0
- R17 pad 1: +5V -> Net-(D1-A)
- R17 pad 2: Net-(U8-VCC) -> /IO0_LED
- R18 pad 1: /DigitalIODriverA1/DIO/5 -> Net-(D13-A)
- R18 pad 2: Net-(U5-+) -> /IO6_LED
- R19 pad 1: /V_{LOGIC}_PORTA -> Net-(D7-A)
- R19 pad 2: /DigitalIODriverA1/V_{LOGIC}/10 -> /IO7_LED
- R2 pad 1: Net-(U2-BOOT) -> /IO1
- R2 pad 2: Net-(C2-Pad1) -> /IOExpander/PB6
- R20 pad 1: /DigitalIODriverA1/V_{LOGIC}/10 -> Net-(D14-A)
- R20 pad 2: GND -> /IO8_LED
- R21 pad 1: Net-(U7-BOOT) -> Net-(D8-A)
- R21 pad 2: Net-(C9-Pad1) -> /IO9_LED
- R22 pad 1: Net-(U8-BOOT) -> Net-(D12-A)
- R22 pad 2: Net-(C11-Pad1) -> /IO11_LED
- R23 pad 1: /DigitalIODriverA0/PULL_PHASE -> Net-(D2-A)
- R23 pad 2: /DIOA0 -> /IO1_LED
- R24 pad 1: /DigitalIODriverA1/DIO_BUFFERED -> Net-(D3-A)
- R24 pad 2: Net-(U9B-+) -> /IO2_LED
- R25 pad 1: Net-(U9B-+) -> Net-(D4-A)
- R25 pad 2: GND -> /IO3_LED
- R27 pad 1: /DigitalIODriverA1/PULL_PHASE -> Net-(D5-A)
- R27 pad 2: /DIOA1 -> /IO4_LED
- R28 pad 1: +5V -> Net-(D6-A)
- R28 pad 2: Net-(D2-A) -> /IO5_LED
- R29 pad 1: /DIG_IN_A2 -> Net-(D15-A)
- R29 pad 2: +5V -> /IO13_LED
- R3 pad 1: +5V -> /IOExpander/PB5
- R3 pad 2: Net-(U2-VCC) -> /IO2
- R30 pad 1: /DIG_IN_A2 -> Net-(D16-A)
- R30 pad 2: Net-(U10-+) -> /IO15_LED
- R31 pad 1: +5V -> Net-(D17-A)
- R31 pad 2: Net-(U11-VCC) -> /IO10_LED
- R32 pad 1: +5V -> Net-(D18-A)
- R32 pad 2: Net-(U12-VCC) -> /IO12_LED
- R33 pad 1: /DigitalIODriverA2/DIO/5 -> Net-(D19-A)
- R33 pad 2: Net-(U10-+) -> /IO14_LED
- R4 pad 1: /DIG_IN_A0 -> /IO3
- R4 pad 2: Net-(U3-+) -> /IOExpander/PB4
- R5 pad 1: /DigitalIODriverA0/DIO/5 -> /IOExpander/PB3
- R5 pad 2: Net-(U3-+) -> /IO4
- R6 pad 1: /DIG_IN_A0 -> /IO5
- R6 pad 2: +5V -> /IOExpander/PB2
- R7 pad 1: Net-(U6B-+) -> /IOExpander/PB1
- R7 pad 2: GND -> /IO6
- R8 pad 1: /DigitalIODriverA0/DIO_BUFFERED -> /IO7
- R8 pad 2: Net-(U6B-+) -> /IOExpander/PB0
- R9 pad 1: /V_{LOGIC}_PORTA -> /IOExpander/PA7
- R9 pad 2: /DigitalIODriverA0/V_{LOGIC}/10 -> /IO8
- U1 pad 1: Net-(U1-BOOT) -> /IO1
- U1 pad 2: /HICUR_LOGIC_CTRL_A0 -> GND
- U1 pad 3: +5V -> /IO0
- U1 pad 4: Net-(U1-VCC) -> /IO2
- U1 pad 5: /DigitalIODriverA0/HICUR_LGATE -> V_{LOGIC}
- U1 pad 6: GND -> /IO3
- U2 pad 1: Net-(U2-BOOT) -> /IO5
- U2 pad 2: /PULL_LOGIC_CTRL_A0 -> GND
- U2 pad 3: +5V -> /IO4
- U2 pad 4: Net-(U2-VCC) -> /IO6
- U2 pad 5: /DigitalIODriverA0/PULL_LGATE -> V_{LOGIC}
- U2 pad 6: GND -> /IO7
- U3 pad 1: GND -> /IO9
- U3 pad 2: Net-(U3-+) -> GND
- U3 pad 3: /DigitalIODriverA0/V_{LOGIC}/10 -> /IO8
- U3 pad 4: GND -> /IO10
- U3 pad 5: unconnected-(U3-BAL-Pad5) -> V_{LOGIC}
- U3 pad 6: unconnected-(U3-STRB-Pad6) -> /IO11
- U35 pad 1: /DIG_IN_A1 -> /IOExpander/PB0
- U35 pad 11: /LevelShifter/~{CS_5V}0 -> /~{CS_VL}0
- U35 pad 12: /IOExpanderA/SPI_5V.SCLK -> /SPI_VL.SCLK
- U35 pad 13: /IOExpanderA/SPI_5V.MOSI -> /SPI_VL.MOSI
- U35 pad 18: /~{RESET_5V} -> /~{RESET_VL}
- U35 pad 2: /PULL_LOGIC_CTRL_A1 -> /IOExpander/PB1
- U35 pad 21: unconnected-(U35-GPA0-Pad21) -> /IOExpander/PA0
- U35 pad 22: unconnected-(U35-GPA1-Pad22) -> /IOExpander/PA1
- U35 pad 23: /DIG_IN_A3 -> /IOExpander/PA2
- U35 pad 24: /PULL_LOGIC_CTRL_A3 -> /IOExpander/PA3
- U35 pad 25: /HICUR_LOGIC_CTRL_A3 -> /IOExpander/PA4
- U35 pad 26: /DIG_IN_A2 -> /IOExpander/PA5
- U35 pad 27: /PULL_LOGIC_CTRL_A2 -> /IOExpander/PA6
- U35 pad 28: /HICUR_LOGIC_CTRL_A2 -> /IOExpander/PA7
- U35 pad 3: /HICUR_LOGIC_CTRL_A1 -> /IOExpander/PB2
- U35 pad 4: /DIG_IN_A0 -> /IOExpander/PB3
- U35 pad 5: /PULL_LOGIC_CTRL_A0 -> /IOExpander/PB4
- U35 pad 6: /HICUR_LOGIC_CTRL_A0 -> /IOExpander/PB5
- U35 pad 7: unconnected-(U35-GPB6-Pad7) -> /IOExpander/PB6
- U35 pad 8: unconnected-(U35-GPB7-Pad8) -> /IOExpander/PB7
- U35 pad 9: +5V -> V_{LOGIC}
- U4 pad 1: /LevelShifter/~{CS_5V}2 -> /~{CS_VL}2
- U4 pad 3: +5V -> V_{LOGIC}
- U4 pad 5: /IOExpanderA/SPI_5V.MOSI -> /SPI_VL.MOSI
- U4 pad 6: /IOExpanderA/SPI_5V.SCLK -> /SPI_VL.SCLK
- U4 pad 7: +5V -> V_{LOGIC}
- U4 pad 8: +5V -> V_{LOGIC}
- U5 pad 1: GND -> /IO13
- U5 pad 2: Net-(U5-+) -> GND
- U5 pad 3: /DigitalIODriverA1/V_{LOGIC}/10 -> /IO12
- U5 pad 4: GND -> /IO14
- U5 pad 5: unconnected-(U5-BAL-Pad5) -> V_{LOGIC}
- U5 pad 6: unconnected-(U5-STRB-Pad6) -> /IO15
- U6 pad 1: /DigitalIODriverA0/DIO_BUFFERED -> /IOExpander/PB7
- U6 pad 2: /DigitalIODriverA0/DIO_BUFFERED -> /IO0_LED
- U6 pad 3: /DIOA0 -> /IOExpander/PB6
- U6 pad 4: GND -> /IO1_LED
- U6 pad 5: Net-(U6B-+) -> /IOExpander/PB5
- U6 pad 6: /DigitalIODriverA0/DIO/5 -> /IO2_LED
- U6 pad 7: /DigitalIODriverA0/DIO/5 -> GND
- U6 pad 8: /V_{LOGIC}_PORTA -> /IO3_LED
- U7 pad 1: Net-(U7-BOOT) -> /~{CS}0
- U7 pad 2: /HICUR_LOGIC_CTRL_A1 -> +3.3V
- U7 pad 3: +5V -> /~{CS}1
- U7 pad 4: Net-(U7-VCC) -> /~{CS}2
- U7 pad 5: /DigitalIODriverA1/HICUR_LGATE -> /SPI.SCLK
- U7 pad 6: GND -> /~{RESET}
- U7 pad 7: /DIOA1 -> /SPI.MOSI
- U7 pad 8: /DigitalIODriverA1/HICUR_UGATE -> +3.3V
- U8 pad 1: Net-(U8-BOOT) -> /IOExpander/PB1
- U8 pad 2: /PULL_LOGIC_CTRL_A1 -> /IO6_LED
- U8 pad 3: +5V -> /IOExpander/PB0
- U8 pad 4: Net-(U8-VCC) -> /IO7_LED
- U8 pad 5: /DigitalIODriverA1/PULL_LGATE -> /IOExpander/PA7
- U8 pad 6: GND -> /IO8_LED
- U8 pad 7: /DigitalIODriverA1/PULL_PHASE -> GND
- U8 pad 8: /DigitalIODriverA1/PULL_UGATE -> /IO9_LED
- U8 pad 9: GND -> /IOExpander/PA6
- U9 pad 1: /DigitalIODriverA1/DIO_BUFFERED -> /IOExpander/PA5
- U9 pad 2: /DigitalIODriverA1/DIO_BUFFERED -> /IO10_LED
- U9 pad 3: /DIOA1 -> /IOExpander/PA4
- U9 pad 4: GND -> /IO11_LED
- U9 pad 5: Net-(U9B-+) -> /IOExpander/PA3
- U9 pad 6: /DigitalIODriverA1/DIO/5 -> /IO12_LED
- U9 pad 7: /DigitalIODriverA1/DIO/5 -> GND
- U9 pad 8: /V_{LOGIC}_PORTA -> /IO13_LED
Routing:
- net V_{LOGIC}: track 0.00 -> 356.7 mm, vias 0 -> 2
- net +V_SUPPLY: track 110.2 -> 0.00 mm
- net /IOExpander/PB7: track 0.00 -> 62.7 mm, vias 0 -> 2
- net /IOExpander/PB6: track 0.00 -> 57.1 mm, vias 0 -> 2
- net /IOExpander/PB4: track 0.00 -> 50.7 mm
- net /IOExpander/PB5: track 0.00 -> 47.0 mm, vias 0 -> 2
- net /IOExpander/PB3: track 0.00 -> 39.6 mm
- net /~{RESET}: track 45.1 -> 8.02 mm, vias 3 -> 0
- net /IOExpander/PB2: track 0.00 -> 36.2 mm, vias 0 -> 2
- net +3.3V: track 29.6 -> 64.9 mm
- net Net-(D6-A): track 0.00 -> 35.3 mm, vias 0 -> 1
- net /SPI_VL.SCLK: track 0.00 -> 34.1 mm
- net Net-(D2-A): track 0.00 -> 32.3 mm, vias 0 -> 1
- net Net-(D1-A): track 0.00 -> 31.4 mm, vias 0 -> 1
- net /LevelShifter/ANY_CS_LOW: track 0.00 -> 30.0 mm
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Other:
- board text added: "+3.3V"
- board text added: "+5V"
- board text added: "Place Jumper to Select V_{LOGIC}"
- board text added: "V_{LOGIC}"
